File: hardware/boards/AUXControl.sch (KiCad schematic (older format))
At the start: 1 part, among them U1 ECP5UM5G-381caBGA

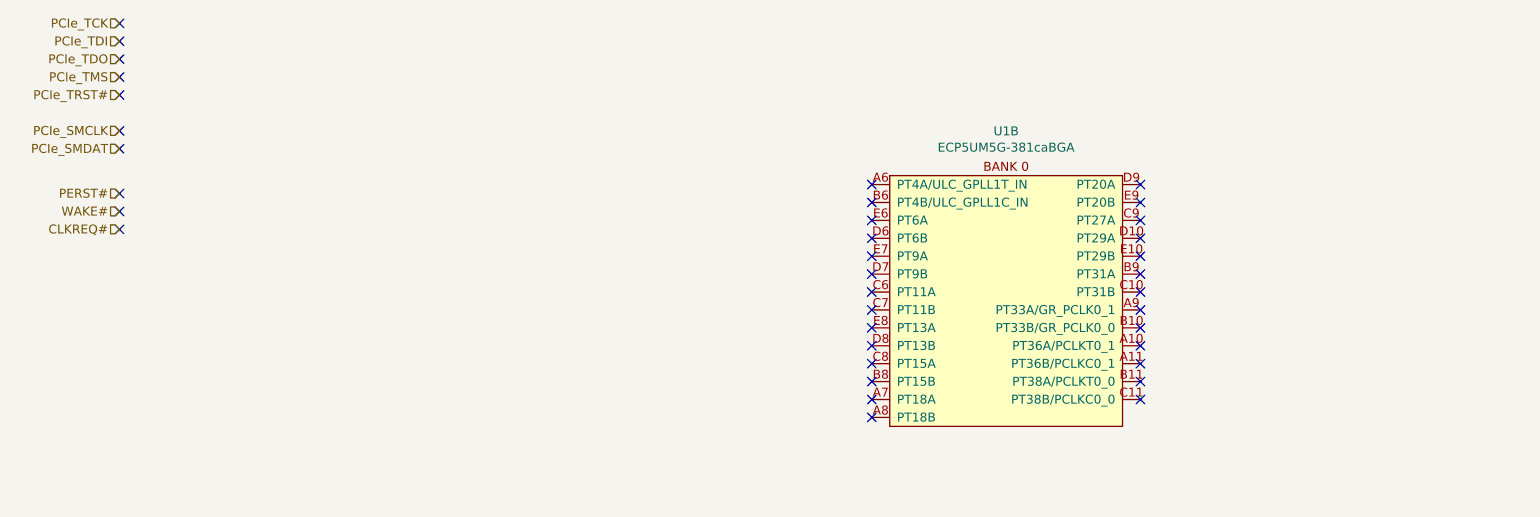
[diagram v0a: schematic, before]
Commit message: Added the main OSC for the FPGA
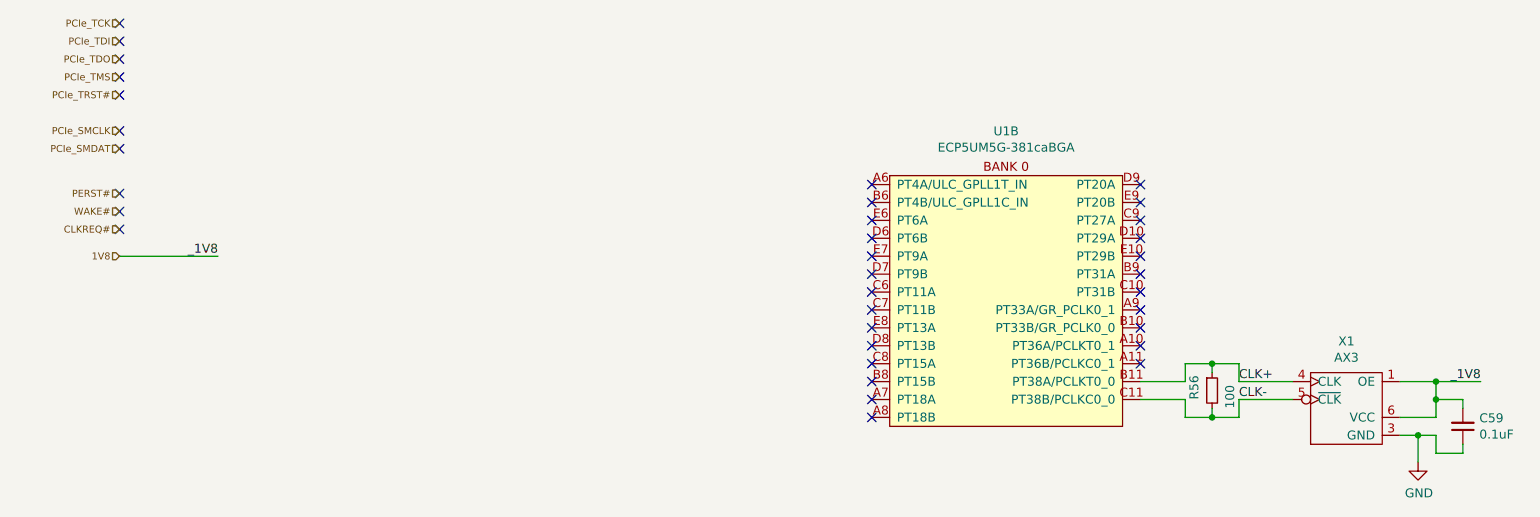
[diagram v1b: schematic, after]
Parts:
- added C59: 0.1uF, Capacitor_SMD:C_0603_1608Metric, symbol Device:C_Small
- added R56: 100, Resistor_SMD:R_0402_1005Metric, symbol Device:R_Small
- added X1: AX3, lethalbit:AX3, symbol lethalbit:AX3
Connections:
- net CLK+: now reaches U1.B11 (PT38A/PCLKT0_0)
- net CLK+: now also R56.1, X1.4 (CLK)
- net CLK-: now reaches U1.C11 (PT38B/PCLKC0_0)
- net CLK-: now also R56.2, X1.5 (~CLK)
- new net 1V8: C59.2, X1.1 (OE), X1.6 (VCC)
- new net GND: C59.1, X1.3 (GND)
- no-connect marks 37 -> 35
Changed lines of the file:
@@
 $Descr A3 16535 11693
 encoding utf-8
-Sheet 9 11
+Sheet 7 11
 Title "lethallink - PCIe Auxiliary Connections"
 Date "2020-06-13"
@@
 Comment4 ""
 $EndDescr
-Text HLabel 1100 750  0    50   Input ~ 0
+Text HLabel 1100 750  0    39   Input ~ 0
 PCIe_TCK
-Text HLabel 1100 850  0    50   Input ~ 0
+Text HLabel 1100 850  0    39   Input ~ 0
 PCIe_TDI
-Text HLabel 1100 950  0    50   Input ~ 0
+Text HLabel 1100 950  0    39   Input ~ 0
 PCIe_TDO
-Text HLabel 1100 1050 0    50   Input ~ 0
+Text HLabel 1100 1050 0    39   Input ~ 0
 PCIe_TMS
-Text HLabel 1100 1150 0    50   Input ~ 0
+Text HLabel 1100 1150 0    39   Input ~ 0
 PCIe_TRST#
-Text HLabel 1100 1350 0    50   Input ~ 0
+Text HLabel 1100 1350 0    39   Input ~ 0
 PCIe_SMCLK
-Text HLabel 1100 1450 0    50   Input ~ 0
+Text HLabel 1100 1450 0    39   Input ~ 0
 PCIe_SMDAT
-Text HLabel 1100 1700 0    50   Input ~ 0
+Text HLabel 1100 1700 0    39   Input ~ 0
 PERST#
-Text HLabel 1100 1800 0    50   Input ~ 0
+Text HLabel 1100 1800 0    39   Input ~ 0
 WAKE#
-Text HLabel 1100 1900 0    50   Input ~ 0
+Text HLabel 1100 1900 0    39   Input ~ 0
 CLKREQ#
 $Comp
@@
 NoConn ~ 6800 2550
 NoConn ~ 6800 2650
-NoConn ~ 6800 2750
-NoConn ~ 6800 2850
 NoConn ~ 1100 750
 NoConn ~ 1100 850
@@
 NoConn ~ 1100 1800
 NoConn ~ 1100 1900
+$Comp
+L lethalbit:AX3 X1
+U 1 1 6117F2EC
+P 7950 2900
+F 0 "X1" H 7950 3275 50  0000 C CNN
+F 1 "AX3" H 7950 3184 50  0000 C CNN
+F 2 "lethalbit:AX3" H 7600 3200 50  0001 C CNN
+F 3 "https://abracon.com/datasheets/AX3.pdf" H 7600 3200 50  0001 C CNN
+F 4 "Abracon LLC" H 7950 2900 50  0001 C CNN "MFR"
+F 5 "AX3DCF1-100.0000" H 7950 2900 50  0001 C CNN "MPN"
+	1    7950 2900
+	-1   0    0    -1
+$EndComp
+$Comp
+L Device:R_Small R56
+U 1 1 61192875
+P 7200 2800
+F 0 "R56" V 7100 2750 50  0000 L CNN
+F 1 "100" V 7300 2700 50  0000 L CNN
+F 2 "Resistor_SMD:R_0402_1005Metric" H 7200 2800 50  0001 C CNN
+F 3 "~" H 7200 2800 50  0001 C CNN
+F 4 "Vishay Dale" H 7200 2800 50  0001 C CNN "MFR"
+F 5 "RCS0402100RFKED" V 7200 2800 50  0001 C CNN "MPN"
+	1    7200 2800
+	1    0    0    -1
+$EndComp
+Wire Wire Line
+	6800 2850 7050 2850
+Wire Wire Line
+	7050 2850 7050 2950
+Wire Wire Line
+	7050 2950 7200 2950
+Wire Wire Line
+	7350 2950 7350 2850
+Wire Wire Line
+	7350 2850 7650 2850
+Wire Wire Line
+	7650 2750 7350 2750
+Wire Wire Line
+	7350 2750 7350 2650
+Wire Wire Line
+	7350 2650 7200 2650
+Wire Wire Line
+	7050 2650 7050 2750
+Wire Wire Line
+	7050 2750 6800 2750
+Wire Wire Line
+	7200 2650 7200 2700
+Connection ~ 7200 2650
+Wire Wire Line
+	7200 2650 7050 2650
+Wire Wire Line
+	7200 2900 7200 2950
+Connection ~ 7200 2950
+Wire Wire Line
+	7200 2950 7350 2950
+$Comp
+L power:GND #PWR0140
+U 1 1 6119E62D
+P 8350 3200
+F 0 "#PWR0140" H 8350 2950 50  0001 C CNN
+F 1 "GND" H 8355 3027 50  0000 C CNN
+F 2 "" H 8350 3200 50  0001 C CNN
+F 3 "" H 8350 3200 50  0001 C CNN
+	1    8350 3200
+	1    0    0    -1
+$EndComp
+Wire Wire Line
+	8250 3050 8350 3050
+Wire Wire Line
+	8350 3050 8350 3200
+$Comp
+L Device:C_Small C?
+U 1 1 611A8322
+P 8600 3000
+AR Path="/5EDF9F51/611A8322" Ref="C?"  Part="1"
+AR Path="/5EDAB834/611A8322" Ref="C59"  Part="1"
+F 0 "C59" H 8508 2954 50  0000 R CNN
+F 1 "0.1uF" H 8508 3045 50  0000 R CNN
+F 2 "Capacitor_SMD:C_0603_1608Metric" H 8600 3000 50  0001 C CNN
+F 3 "~" H 8600 3000 50  0001 C CNN
+F 4 "KEMET" V 8600 3000 50  0001 C CNN "MFR"
+F 5 "C0603C104M5RACTU" V 8600 3000 50  0001 C CNN "MPN"
+	1    8600 3000
+	-1   0    0    1
+$EndComp
+Wire Wire Line
+	8350 3050 8450 3050
+Wire Wire Line
+	8450 3050 8450 3150
+Wire Wire Line
+	8450 3150 8600 3150
+Wire Wire Line
+	8600 3150 8600 3100
+Connection ~ 8350 3050
+Wire Wire Line
+	8250 2950 8450 2950
+Wire Wire Line
+	8450 2950 8450 2850
+Wire Wire Line
+	8450 2850 8600 2850
+Wire Wire Line
+	8600 2850 8600 2900
+Wire Wire Line
+	8250 2750 8450 2750
+Wire Wire Line
+	8450 2750 8450 2850
+Connection ~ 8450 2850
+Wire Wire Line
+	8450 2750 8700 2750
+Connection ~ 8450 2750
+Text Label 8700 2750 2    50   ~ 0
+_1V8
+Text HLabel 1100 2050 0    39   Input ~ 0
+1V8
+Wire Wire Line
+	1100 2050 1650 2050
+Text Label 1650 2050 2    50   ~ 0
+_1V8
+Text Label 7350 2750 0    50   ~ 0
+CLK+
+Text Label 7350 2850 0    50   ~ 0
+CLK-
 $EndSCHEMATC

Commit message: Moved some more banks around to try and keeps things from crossing over as much as possible
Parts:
- removed C59: 0.1uF, Capacitor_SMD:C_0603_1608Metric, symbol Device:C_Small
- removed R56: 100, Resistor_SMD:R_0402_1005Metric, symbol Device:R_Small
- removed U1: ECP5UM5G-381caBGA, lethalbit:318caBGA, symbol lethalbit:ECP5UM5G-381caBGA
- removed X1: AX3, lethalbit:AX3, symbol lethalbit:AX3
- added U1: ECP5UM5G-381caBGA, lethalbit:318caBGA, symbol lethalbit:ECP5UM5G-381caBGA
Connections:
- no-connect marks 35 -> 43
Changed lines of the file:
@@
 Text HLabel 1100 1900 0    39   Input ~ 0
 CLKREQ#
-$Comp
-L lethalbit:ECP5UM5G-381caBGA U1
-U 2 1 5F965335
-P 6050 1700
-F 0 "U1" H 6050 2048 50  0000 C CNN
-F 1 "ECP5UM5G-381caBGA" H 6050 1957 50  0000 C CNN
-F 2 "lethalbit:318caBGA" H 4700 1850 50  0001 C CNN
-F 3 "" H 4700 1850 50  0001 C CNN
-F 4 "Lattice" H 6050 1700 50  0001 C CNN "MFR"
-F 5 "LFE5UM5G-85F-8BG381I" H 6050 1700 50  0001 C CNN "MPN"
-F 6 "220-2112-ND" H 6050 1700 50  0001 C CNN "DIGIKEY_PN"
-	2    6050 1700
-	1    0    0    -1
-$EndComp
-NoConn ~ 5300 1650
-NoConn ~ 5300 1750
-NoConn ~ 5300 1850
-NoConn ~ 5300 1950
-NoConn ~ 5300 2050
-NoConn ~ 5300 2150
-NoConn ~ 5300 2250
-NoConn ~ 5300 2350
-NoConn ~ 5300 2450
-NoConn ~ 5300 2550
-NoConn ~ 5300 2650
-NoConn ~ 5300 2750
-NoConn ~ 5300 2850
-NoConn ~ 5300 2950
+NoConn ~ 5000 1650
+NoConn ~ 5000 1750
+NoConn ~ 5000 1850
+NoConn ~ 5000 1950
+NoConn ~ 5000 2050
+NoConn ~ 5000 2150
+NoConn ~ 5000 2250
+NoConn ~ 5000 2350
+NoConn ~ 5000 2450
+NoConn ~ 5000 2550
+NoConn ~ 5000 2650
+NoConn ~ 5000 2750
+NoConn ~ 5000 2850
+NoConn ~ 5000 2950
 NoConn ~ 6800 1650
 NoConn ~ 6800 1750
@@
 NoConn ~ 1100 1900
 $Comp
-L lethalbit:AX3 X1
-U 1 1 6117F2EC
-P 7950 2900
-F 0 "X1" H 7950 3275 50  0000 C CNN
-F 1 "AX3" H 7950 3184 50  0000 C CNN
-F 2 "lethalbit:AX3" H 7600 3200 50  0001 C CNN
-F 3 "https://abracon.com/datasheets/AX3.pdf" H 7600 3200 50  0001 C CNN
-F 4 "Abracon LLC" H 7950 2900 50  0001 C CNN "MFR"
-F 5 "AX3DCF1-100.0000" H 7950 2900 50  0001 C CNN "MPN"
-	1    7950 2900
+L lethalbit:ECP5UM5G-381caBGA U?
+U 6 1 5FD7443A
+P 5900 1700
+AR Path="/5EDF3898/5FD7443A" Ref="U?"  Part="6"
+AR Path="/5FD7443A" Ref="U?"  Part="6"
+AR Path="/5EF6A128/5FD7443A" Ref="U?"  Part="6"
+AR Path="/5F2CAFD2/5FD7443A" Ref="U?"  Part="6"
+AR Path="/5EDAB834/5FD7443A" Ref="U1"  Part="6"
+F 0 "U1" H 5900 2048 50  0000 C CNN
+F 1 "ECP5UM5G-381caBGA" H 5900 1957 50  0000 C CNN
+F 2 "lethalbit:318caBGA" H 4550 1850 50  0001 C CNN
+F 3 "" H 4550 1850 50  0001 C CNN
+F 4 "Lattice" H 5900 1700 50  0001 C CNN "MFR"
+F 5 "LFE5UM5G-85F-8BG381I" H 5900 1700 50  0001 C CNN "MPN"
+F 6 "220-2112-ND" H 5900 1700 50  0001 C CNN "DIGIKEY_PN"
+	6    5900 1700
 	-1   0    0    -1
 $EndComp
-$Comp
-L Device:R_Small R56
-U 1 1 61192875
-P 7200 2800
-F 0 "R56" V 7100 2750 50  0000 L CNN
-F 1 "100" V 7300 2700 50  0000 L CNN
-F 2 "Resistor_SMD:R_0402_1005Metric" H 7200 2800 50  0001 C CNN
-F 3 "~" H 7200 2800 50  0001 C CNN
-F 4 "Vishay Dale" H 7200 2800 50  0001 C CNN "MFR"
-F 5 "RCS0402100RFKED" V 7200 2800 50  0001 C CNN "MPN"
-	1    7200 2800
-	1    0    0    -1
-$EndComp
-Wire Wire Line
-	6800 2850 7050 2850
-Wire Wire Line
-	7050 2850 7050 2950
-Wire Wire Line
-	7050 2950 7200 2950
-Wire Wire Line
-	7350 2950 7350 2850
-Wire Wire Line
-	7350 2850 7650 2850
-Wire Wire Line
-	7650 2750 7350 2750
-Wire Wire Line
-	7350 2750 7350 2650
-Wire Wire Line
-	7350 2650 7200 2650
-Wire Wire Line
-	7050 2650 7050 2750
-Wire Wire Line
-	7050 2750 6800 2750
-Wire Wire Line
-	7200 2650 7200 2700
-Connection ~ 7200 2650
-Wire Wire Line
-	7200 2650 7050 2650
-Wire Wire Line
-	7200 2900 7200 2950
-Connection ~ 7200 2950
-Wire Wire Line
-	7200 2950 7350 2950
-$Comp
-L power:GND #PWR0140
-U 1 1 6119E62D
-P 8350 3200
-F 0 "#PWR0140" H 8350 2950 50  0001 C CNN
-F 1 "GND" H 8355 3027 50  0000 C CNN
-F 2 "" H 8350 3200 50  0001 C CNN
-F 3 "" H 8350 3200 50  0001 C CNN
-	1    8350 3200
-	1    0    0    -1
-$EndComp
-Wire Wire Line
-	8250 3050 8350 3050
-Wire Wire Line
-	8350 3050 8350 3200
-$Comp
-L Device:C_Small C?
-U 1 1 611A8322
-P 8600 3000
-AR Path="/5EDF9F51/611A8322" Ref="C?"  Part="1"
-AR Path="/5EDAB834/611A8322" Ref="C59"  Part="1"
-F 0 "C59" H 8508 2954 50  0000 R CNN
-F 1 "0.1uF" H 8508 3045 50  0000 R CNN
-F 2 "Capacitor_SMD:C_0603_1608Metric" H 8600 3000 50  0001 C CNN
-F 3 "~" H 8600 3000 50  0001 C CNN
-F 4 "KEMET" V 8600 3000 50  0001 C CNN "MFR"
-F 5 "C0603C104M5RACTU" V 8600 3000 50  0001 C CNN "MPN"
-	1    8600 3000
-	-1   0    0    1
-$EndComp
-Wire Wire Line
-	8350 3050 8450 3050
-Wire Wire Line
-	8450 3050 8450 3150
-Wire Wire Line
-	8450 3150 8600 3150
-Wire Wire Line
-	8600 3150 8600 3100
-Connection ~ 8350 3050
-Wire Wire Line
-	8250 2950 8450 2950
-Wire Wire Line
-	8450 2950 8450 2850
-Wire Wire Line
-	8450 2850 8600 2850
-Wire Wire Line
-	8600 2850 8600 2900
-Wire Wire Line
-	8250 2750 8450 2750
-Wire Wire Line
-	8450 2750 8450 2850
-Connection ~ 8450 2850
-Wire Wire Line
-	8450 2750 8700 2750
-Connection ~ 8450 2750
-Text Label 8700 2750 2    50   ~ 0
-_1V8
-Text HLabel 1100 2050 0    39   Input ~ 0
-1V8
-Wire Wire Line
-	1100 2050 1650 2050
-Text Label 1650 2050 2    50   ~ 0
-_1V8
-Text Label 7350 2750 0    50   ~ 0
-CLK+
-Text Label 7350 2850 0    50   ~ 0
-CLK-
+NoConn ~ 5000 3050
+NoConn ~ 5000 3150
+NoConn ~ 6800 2750
+NoConn ~ 6800 2850
+NoConn ~ 6800 2950
+NoConn ~ 6800 3050
+NoConn ~ 6800 3150
+NoConn ~ 6800 3250
 $EndSCHEMATC
